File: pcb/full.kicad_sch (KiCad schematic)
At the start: 118 parts, among them J1 MJ-4PP-9, J2 MJ-4PP-9, SW1 SW_PUSH, SW10 SW_PUSH, SW11 SW_PUSH, SW12 SW_PUSH, SW13 SW_PUSH, SW14 SW_PUSH, SW15 SW_PUSH, SW16 SW_PUSH, SW17 SW_PUSH, SW18 SW_PUSH, SW19 SW_PUSH, SW2 SW_PUSH, SW20 SW_PUSH, SW21 SW_PUSH, SW22 SW_PUSH, SW23 SW_PUSH, SW24 SW_PUSH, SW25 SW_PUSH, SW26 SW_PUSH, SW27 SW_PUSH, SW28 SW_PUSH, SW29 SW_PUSH, SW3 SW_PUSH, SW30 SW_PUSH, SW31 SW_PUSH, SW32 SW_PUSH, SW33 SW_PUSH, SW34 SW_PUSH, SW35 SW_PUSH, SW36 SW_PUSH, SW37 SW_PUSH, SW38 SW_PUSH, SW39 SW_PUSH, SW4 SW_PUSH, SW40 SW_PUSH, SW5 SW_PUSH, SW6 SW_PUSH, SW7 SW_PUSH, SW8 SW_PUSH, SW9 SW_PUSH, U1 xiao-ble, U2 xiao-ble

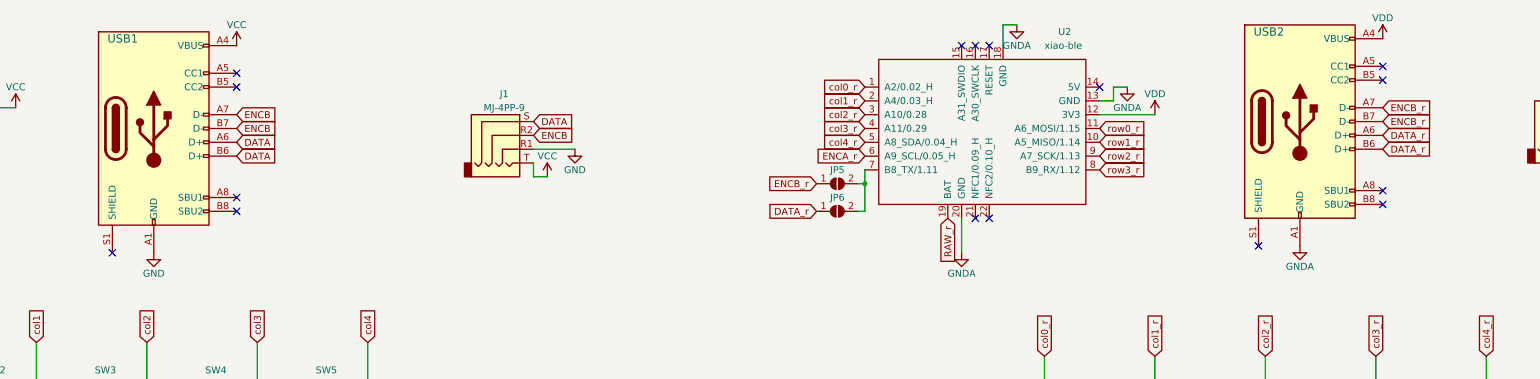
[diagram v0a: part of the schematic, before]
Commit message: top-mount usb-c
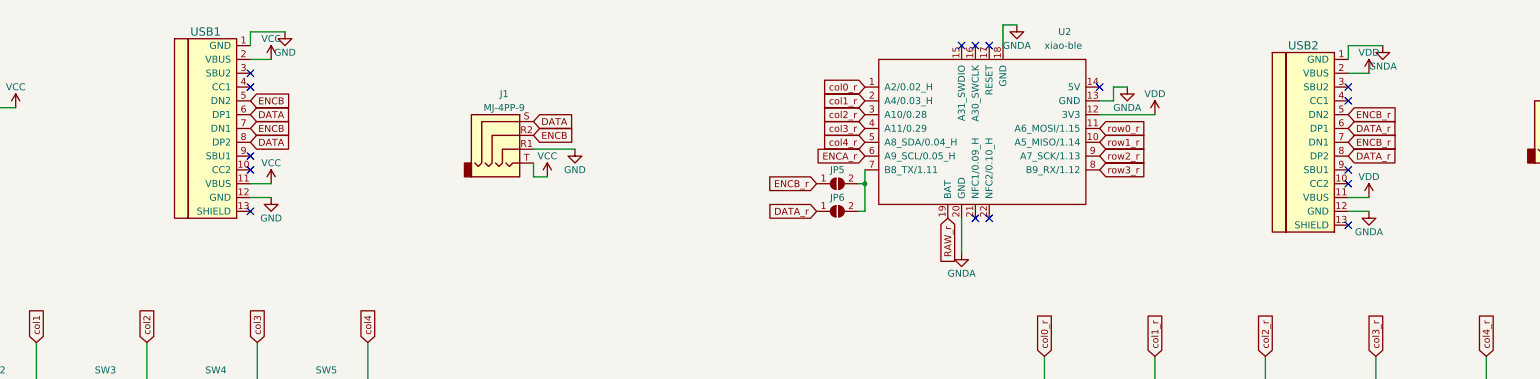
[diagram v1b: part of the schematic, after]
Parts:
- removed USB1, USB2: HRO-TYPE-C-31-M-12, zzkeeb:Connector_USB-C-mid-mount-ali-data, symbol Connector:USB_C_Receptacle_USB2.0
- added USB1, USB2: HRO-TYPE-C-31-M-12, zzkeeb:Connector_HRO-TYPE-C-31-M-12-data, symbol zzkeeb:Connector_HRO-TYPE-C-31-M-12
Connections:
- net DATA: now also USB1.6 (DP1), USB1.8 (DP2)
- net DATA_r: now also USB2.6 (DP1), USB2.8 (DP2)
- net ENCB: now also USB1.5 (DN2), USB1.7 (DN1)
- net ENCB_r: now also USB2.5 (DN2), USB2.7 (DN1)
- net GND: now also USB1.1 (GND), USB1.12 (GND)
- net GNDA: now also USB2.1 (GND), USB2.12 (GND)
- net VCC: now also USB1.11 (VBUS), USB1.2 (VBUS)
- net VDD: now also USB2.11 (VBUS), USB2.2 (VBUS)

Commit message: v2.2
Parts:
- D1, D10, D11, D12, D13, D14, D15, D16, D17, D18, D19, D2, D20, D21, D22, D23, D24, D25, D26, D27, D28, D29, D3, D30, D31, D32, D33, D34, D35, D36, D37, D38, D39, D4, D40, D5, D6, D7, D8, D9: footprint zzkeeb:Diode_1N4148-SOD123 -> zzkeeb:Diode_1N4148-SOD123-no-rowcol
